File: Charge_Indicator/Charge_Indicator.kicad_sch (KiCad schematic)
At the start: 40 parts, among them J1 1984617

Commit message: Adding some more text to the schematic
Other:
- note added: "Battery Voltage Level [25.6 <-> 20.0]V"
- note added: "LM393 [NEEDS TO BE MADE]"
- note added: "SGM61410XN6G/TR [NEEDS TO BE MADE]"
- note removed: "Battery Voltage Level"
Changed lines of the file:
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@@
+		)
+	)
+	(text "LM393         [NEEDS TO BE MADE]"
+		(exclude_from_sim no)
+		(at 92.71 92.964 0)
+		(effects
+			(font
+				(size 1.27 1.27)
+			)
 		)
 	)
@@
 		(exclude_from_sim no)
 		(at 108.204 68.834 90)
+		(effects
+			(font
+				(size 1.27 1.27)
+			)
+		)
+	)
+	(text "SGM61410XN6G/TR  [NEEDS TO BE MADE]"
+		(exclude_from_sim no)
+		(at 96.52 90.678 0)
 		(effects
 			(font
@@
 		)
 	)
-	(text "Battery Voltage Level"
+	(text "Battery Voltage Level [25.6 <-> 20.0]V"
 		(exclude_from_sim no)
 		(at 148.336 41.148 0)
@@
 		)
 	)
+	(text_box "Collaboration with Wavenumber LLC Ensure WN logo is on PCB silk layer"
+		(exclude_from_sim no)
+		(at 78.74 30.48 0)
+		(size 38.1 7.62)
+		(margins 0.9525 0.9525 0.9525 0.9525)
+		(stroke
+			(width 0)
+			(type solid)
+			(color 255 232 188 1)
+		)
+		(fill
+			(type color)
+			(color 255 242 154 1)
+		)
+		(effects
+			(font
+				(size 1.27 1.27)
+			)
+			(justify left top)
+		)
+	)
 	(junction
 		(at 190.5 41.91)
@@
 			(width 0)
 			(type default)
+			(color 255 157 40 1)
 		)
 	)
@@
 			(width 0)
 			(type default)
+			(color 255 129 30 1)
 		)
 	)
@@
 			(width 0)
 			(type default)
+			(color 255 157 40 1)
 		)
 	)
@@
 			(width 0)
 			(type default)
+			(color 255 129 30 1)
 		)
 	)
@@
 			(width 0)
 			(type default)
+			(color 255 157 40 1)
 		)
 	)
@@
 			(width 0)
 			(type default)
+			(color 255 129 30 1)
 		)
 	)
@@
 			(width 0)
 			(type default)
+			(color 255 129 30 1)
 		)
 	)
@@
 			(width 0)
 			(type default)
+			(color 255 129 30 1)
 		)
 	)
@@
 			(width 0)
 			(type default)
+			(color 255 129 30 1)
 		)
 	)
@@
 			(width 0)
 			(type default)
+			(color 255 157 40 1)
 		)
 	)
@@
 			(width 0)
 			(type default)
+			(color 255 157 40 1)
 		)
 	)
@@
 			(width 0)
 			(type default)
+			(color 255 157 40 1)
 		)
 	)
@@
 			(width 0)
 			(type default)
+			(color 255 157 40 1)
 		)
 	)
@@
 			(width 0)
 			(type default)
+			(color 255 157 40 1)
 		)
 	)
@@
 			(width 0)
 			(type default)
+			(color 255 157 40 1)
 		)
 	)
@@
 			(width 0)
 			(type default)
+			(color 255 157 40 1)
 		)
 	)
@@
 			(width 0)
 			(type default)
+			(color 255 129 30 1)
 		)
 	)
@@
 			(width 0)
 			(type default)
+			(color 255 129 30 1)
 		)
 	)
@@
 			(width 0)
 			(type default)
+			(color 255 157 40 1)
 		)
 	)
@@
 			(width 0)
 			(type default)
+			(color 255 157 40 1)
 		)
 	)
@@
 			(width 0)
 			(type default)
+			(color 255 129 30 1)
 		)
 	)
@@
 			(width 0)
 			(type default)
+			(color 255 129 30 1)
 		)
 	)
@@
 			(width 0)
 			(type default)
+			(color 255 129 30 1)
 		)
 	)
@@
 			(width 0)
 			(type default)
+			(color 255 157 40 1)
 		)
 	)
@@
 			(width 0)
 			(type default)
-		)
-	)
+			(color 255 129 30 1)
+		)
+	)

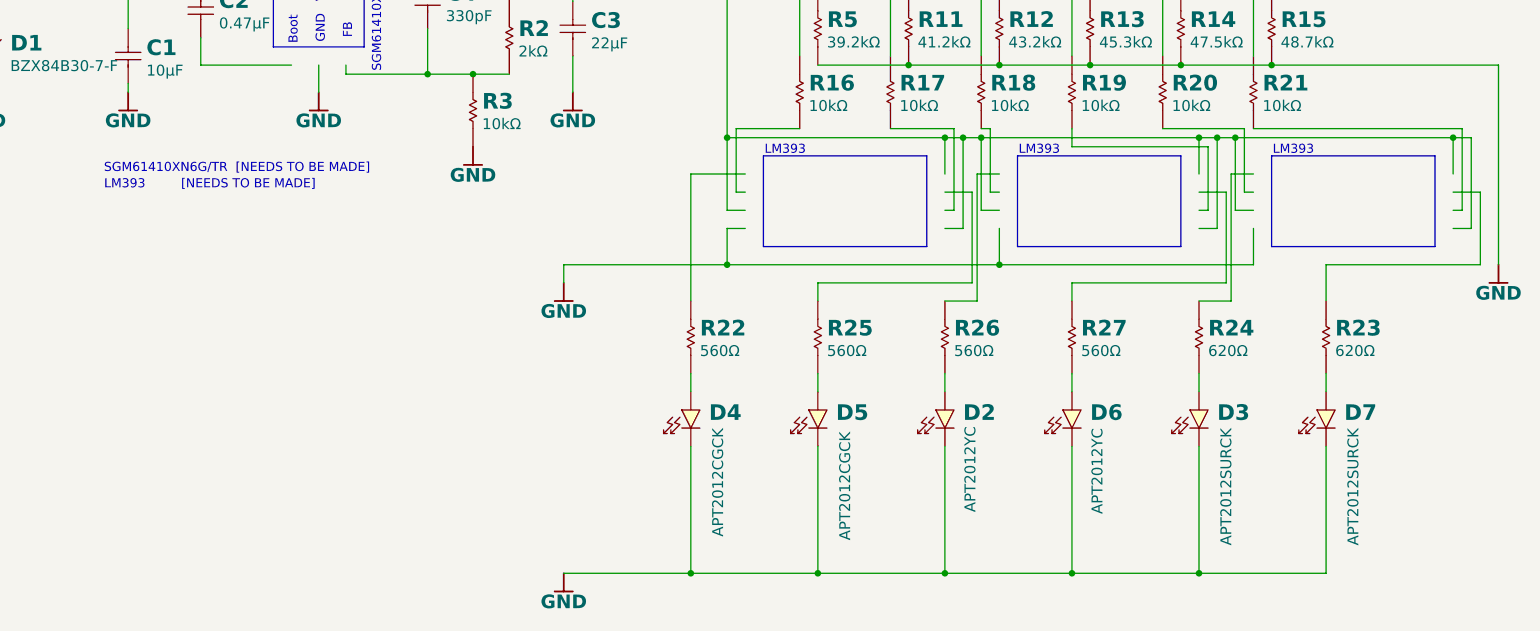
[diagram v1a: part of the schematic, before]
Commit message: Adding pull ups, reversing logic, adding simulation validation image
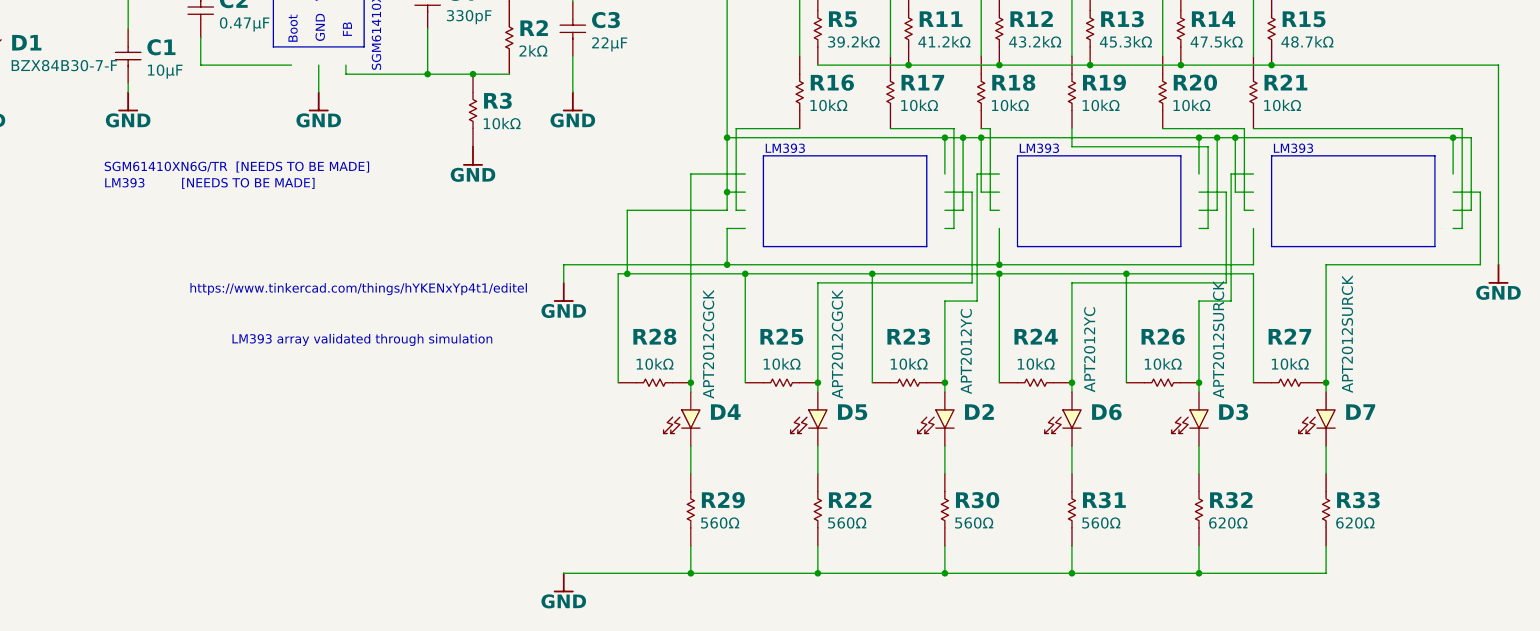
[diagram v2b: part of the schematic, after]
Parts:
- added R28: 10kΩ, wavenumber:R0603_0.55MM_HD, symbol wn__wavenumber:R_2P
- added R29, R30, R31: 560Ω, wavenumber:R0603_0.55MM_HD, symbol wn__wavenumber:R_2P
- added R32, R33: 620Ω, wavenumber:R0603_0.55MM_HD, symbol wn__wavenumber:R_2P
- R23, R24: value 620Ω -> 10kΩ; Manufacturer Part Number ERJ-3EKF6200V -> ERJ-3EKF1002V; cad-reference ERJ-3EKF6200V -> ERJ-3EKF1002V
- R25, R26, R27: value 560Ω -> 10kΩ; Manufacturer Part Number ERJ-3EKF5600V -> ERJ-3EKF1002V; cad-reference ERJ-3EKF5600V -> ERJ-3EKF1002V
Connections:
- net GND: now also R22.1, R29.1, R30.1, R31.1, R32.1, R33.1; no longer D2.C, D3.C, D4.C, D5.C, D6.C, D7.C
- net at D5.A: now also R25.2; no longer R25.1
- net at D6.A: now also R24.2; no longer R27.1
- net at D7.A: now also R27.2; no longer R23.1
- net at D2.A: now also R23.2; no longer R26.1
- net at D4.A: now also R28.2; no longer R22.1
- net at R22.2: now also D5.C
- net at C3.1, C4.1, L2.2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: now also R23.1, R24.1, R25.1, R26.1, R27.1, R28.1
- net at D3.A: now also R26.2; no longer R24.1
- new net: D6.C, R31.2
- new net: D7.C, R33.2
- new net: D4.C, R29.2
- new net: D2.C, R30.2
- new net: D3.C, R32.2
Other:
- note added: "LM393 array validated through simulation"
- note added: "https://www.tinkercad.com/things/hYKENxYp4t1/editel"

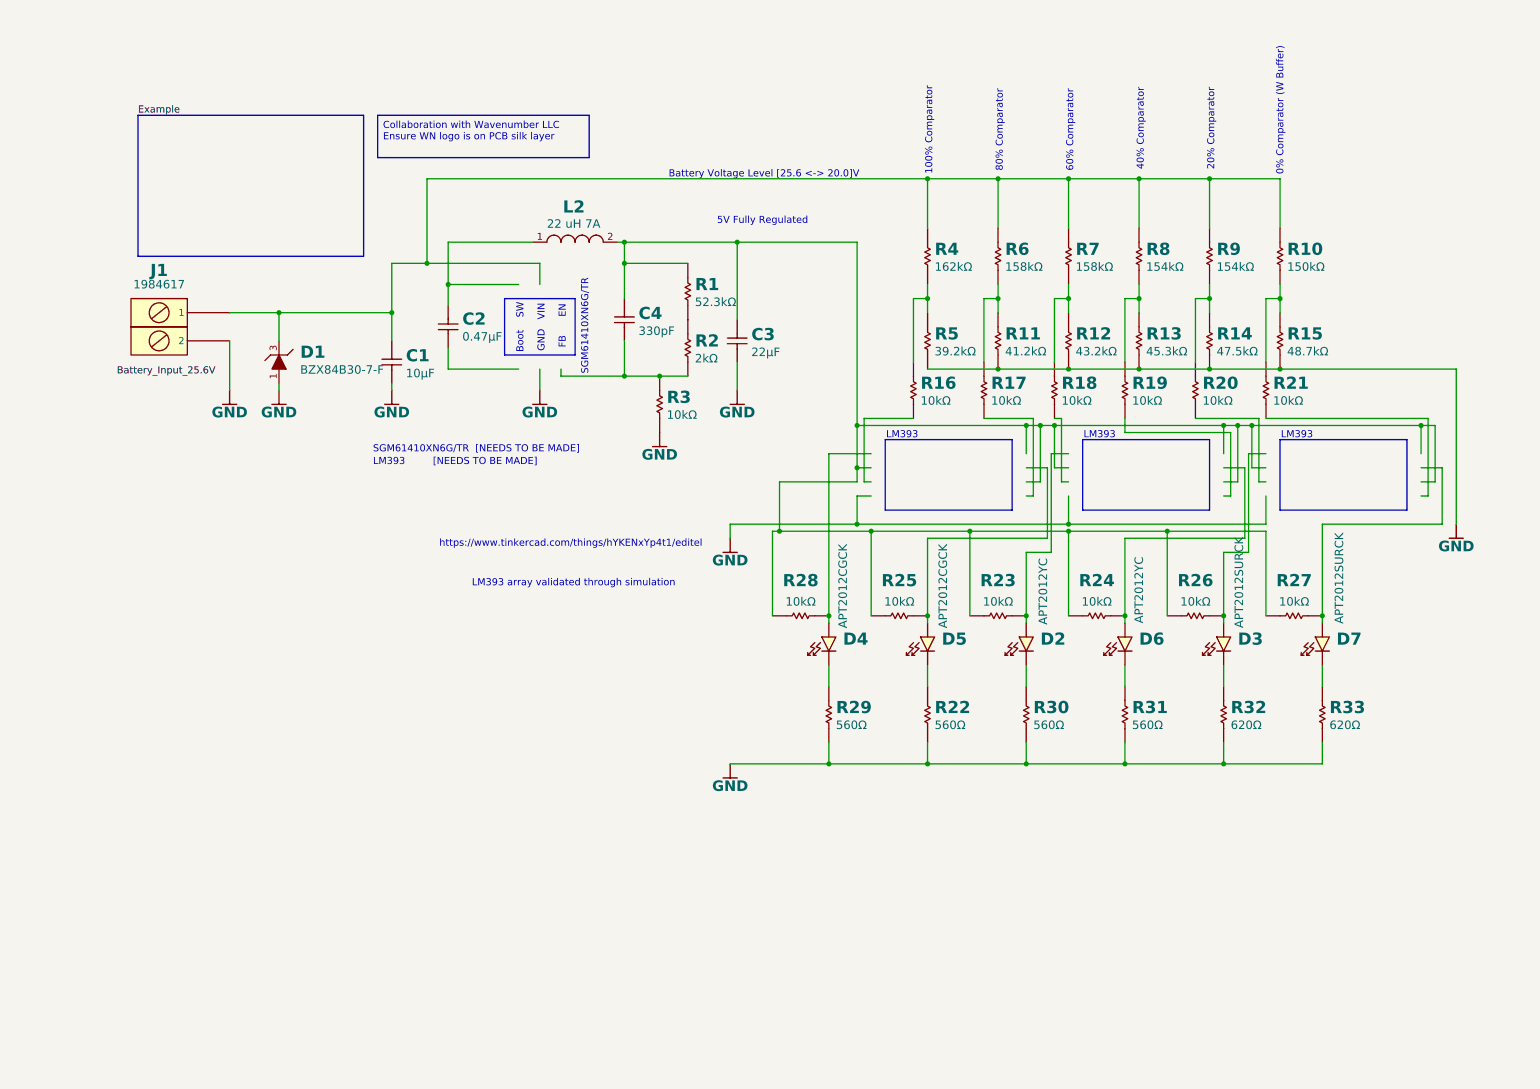
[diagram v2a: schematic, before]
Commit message: Adding KiCad generated symbols for SMT components
Summary of changes:
- Adding in the kicad_mod and kicad_sym of each of the components.
- (might be errors with how these libraries are linked up from the local dir)
- Fixed a wrong resistor in the schematic.
- Moved around graphics.
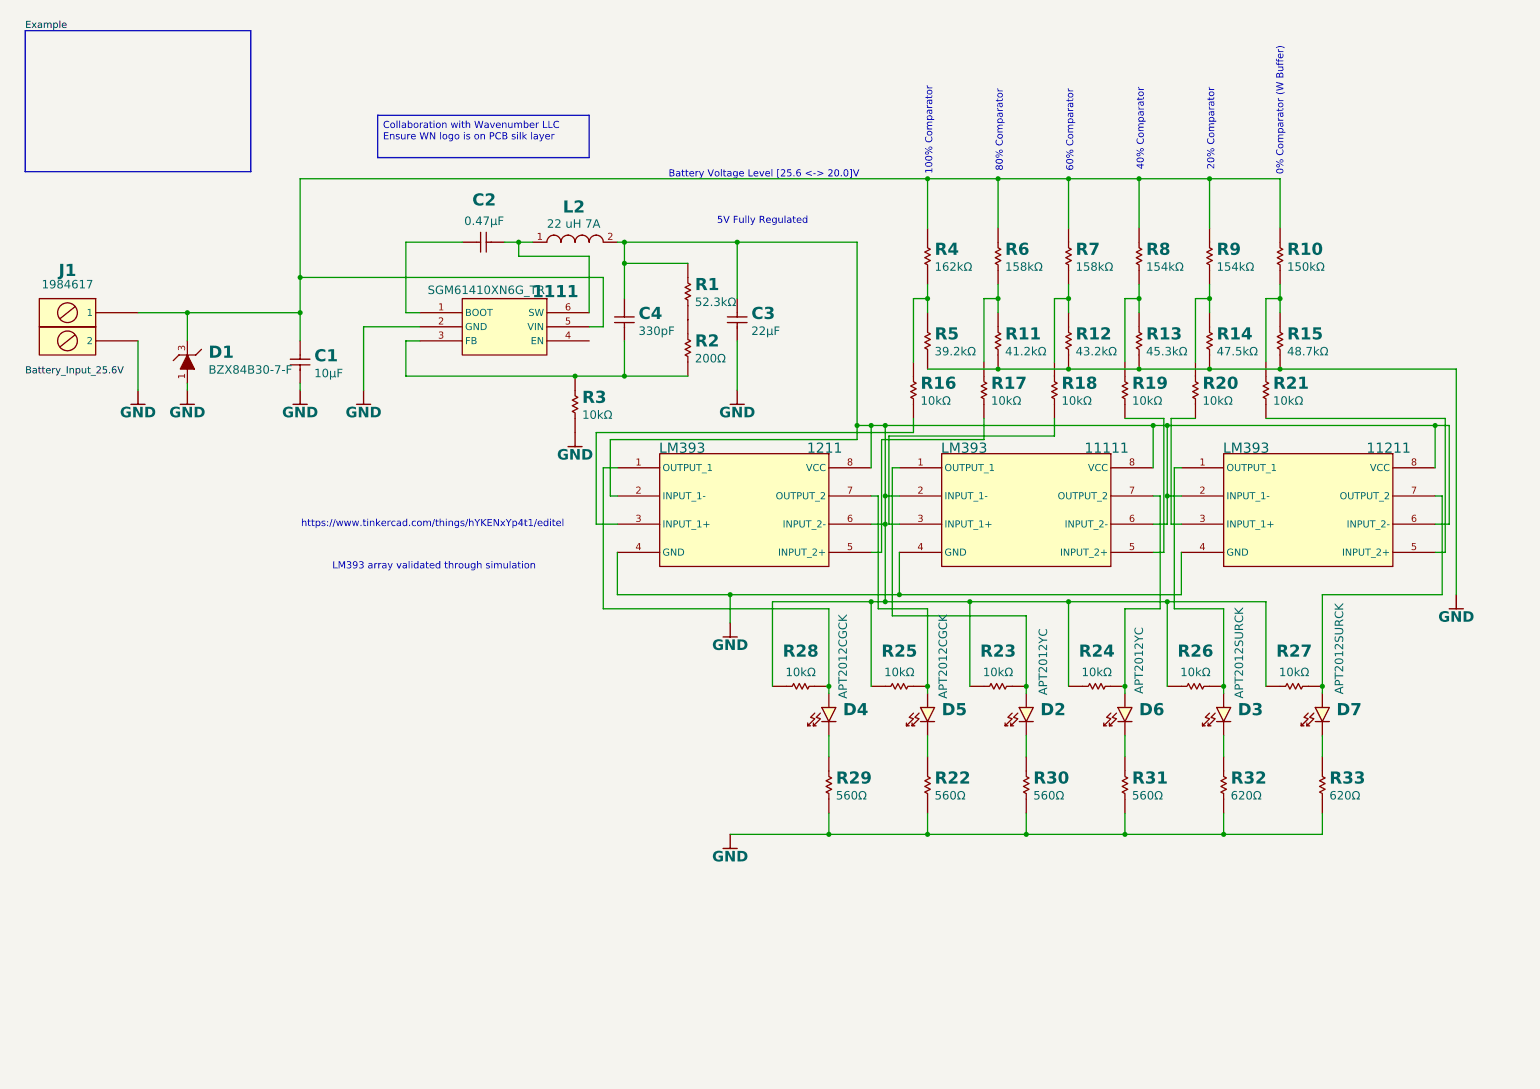
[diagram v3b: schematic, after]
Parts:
- added 1111: SGM61410XN6G_TR, wavenumber:SGM61410XN6G_TR, symbol wn__wavenumber:SGM61410XN6G_TR
- added 11111, 11211, 1211: LM393, wavenumber:LM393, symbol wn__wavenumber:LM393
- R2: value 2kΩ -> 200Ω; Manufacturer Part Number ERJ-3EKF2001V -> ERJ-3EKF2000V; cad-reference ERJ-3EKF2001V -> ERJ-3EKF2000V
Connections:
- net GND: now also 1111.2 (GND), 11111.4 (GND), 11211.4 (GND), 1211.4 (GND)
- net at D5.A, R25.2: now also 1211.7 (OUTPUT_2)
- net at D6.A, R24.2: now also 11111.7 (OUTPUT_2)
- net at D7.A, R27.2: now also 11211.7 (OUTPUT_2)
- net at R16.2: now also 1211.3 (INPUT_1+)
- net at D2.A, R23.2: now also 11111.1 (OUTPUT_1)
- net at C1.1, D1.3 (K), J1.1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: now also 1111.5 (VIN)
- net at C3.1, C4.1, L2.2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: now also 11111.2 (INPUT_1-), 11111.6 (INPUT_2-), 11111.8 (VCC), 11211.2 (INPUT_1-), 11211.6 (INPUT_2-), 11211.8 (VCC), 1211.2 (INPUT_1-), 1211.6 (INPUT_2-), 1211.8 (VCC)
- net at R20.2: now also 11211.3 (INPUT_1+)
- net at C4.2 (1), R2.2, R3.1: now also 1111.3 (FB)
- net at D3.A, R26.2: now also 11211.1 (OUTPUT_1)
- net at R17.2: now also 1211.5 (INPUT_2+)
- net at D4.A, R28.2: now also 1211.1 (OUTPUT_1)
- net at C2.1: now also 1111.1 (BOOT)
- net at C2.2 (1), L2.1: now also 1111.6 (SW)
- net at R19.2: now also 11111.5 (INPUT_2+)
- net at R18.2: now also 11111.3 (INPUT_1+)
- net at R21.2: now also 11211.5 (INPUT_2+)
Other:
- note removed: "Boot SW"
- note removed: "FB EN"
- note removed: "GND VIN"
- note removed: "LM393"
- note removed: "LM393 [NEEDS TO BE MADE]"
- note removed: "SGM61410XN6G/TR"
- note removed: "SGM61410XN6G/TR [NEEDS TO BE MADE]"
- moved on the sheet: C1, C2, C3, D1, D2, D3, D4, D5, D6, D7, J1, R22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
